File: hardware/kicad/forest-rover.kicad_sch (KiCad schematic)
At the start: 0 parts

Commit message: Refine repo wording and KiCad scaffolding
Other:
- note added: "1. Power Management"
- note added: "2. MCU Core"
- note added: "3. Motor Control"
- note added: "4. Sensor Interfaces"
- note added: "5. Communication"
- note added: "6. Connectors and Misc"
- note added: "Analog front-end: PIR buffer, threshold comparator, thermistor divider to ADC"
- note added: "Bring-up checklist: ERC cleanup, connector pinout review, footprint verification, power-tree annotation"
- note added: "Companion compute link: CM4 UART, shared I2C, GPIO interrupt, USB-C for power/data"
- note added: "DRV8871 x2 for two DC gear motors, PWM from STM32 timers, current-sense resistors, Schottky clamps"
- note added: "Encoder path: differential receiver front-end for two quadrature channels"
- note added: "I2C bus devices: BME280 and BNO055 with 4.7k pull-ups to 3.3V"
- note added: "Interfaces: UART1->CM4, UART2->LoRa, SPI1->W25Q128, I2C1->sensor bus, ADC->battery/current/temp"
- note added: "Key notes: input reverse-polarity MOSFET, 2A charge-current limit, LC output filter, soft-start"
- note added: "Layout intent: keep high di/dt loops local to the battery-side motor zone"
- note added: "Off-board headers: LIDAR UART JST-4 and thermal camera JST-6"
- note added: "Power integrity: 100nF per VDD pin plus 4.7uF bulk near MCU core rails"
- note added: "Primary rails: VBAT, +5V, +3V3, MOTOR_VBAT"
- note added: "RF placement intent: module and SMA at board edge with controlled return path"
- note added: "RFM95W LoRa module on SPI, edge-mount SMA, PI matching network, interrupt/DIO routing to MCU"
- note added: "STM32F407VGT6, 8MHz HSE, 32.768kHz LSE, SWD 2x5 1.27mm, BOOT0 jumper, GPIO expansion header"
- note added: "Status LEDs: power, charging, fault, comms; latching pushbutton; four M3 mounting holes"
- note added: "This schematic remains a structured concept. Replace each block with captured circuitry before fabrication."
- note added: "XT60 battery input, solar terminal, LT3652-style charger, TPS54331 5V buck, AMS1117-3.3, TPS2596 motor eFuse"
- note removed: "1. Power Management: solar input, LT3652-style MPPT, TPS54331 buck, AMS1117 LDO, TPS2596 motor eFuse"
- note removed: "2. MCU Core: STM32F407VGT6, crystals, SWD, BOOT0, UART/SPI/I2C/ADC breakouts"
- note removed: "3. Motor Control: DRV8871 x2, current sense, encoder receiver inputs"
- note removed: "4. Sensor Interfaces: BME280, BNO055, PIR analog front-end, thermistor divider, JST sensor headers"
- note removed: "5. Communication: RFM95W + SMA + PI match placeholder, CM4 UART/I2C/INT/USB-C"
- note removed: "6. Connectors and Misc: XT60, solar terminal, LEDs, switch, mounting holes"
- note removed: "Hierarchical block plan:"
- note removed: "This file is a hand-authored KiCad scaffold and should be replaced with a full schematic during capture."
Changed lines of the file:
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@@
   (version 20230121)
   (generator "codex")
-  (uuid "5c8ae4a4-f6bb-4f43-a6ef-forest-rover-sch")
   (paper "A3")
   (title_block
@@
     (company "Team Onyx India")
     (rev "A")
-    (comment 1 "Simplified portfolio schematic scaffold")
-    (comment 2 "Blocks: power, MCU, motors, sensors, comms"))
-  (sheet_instances
-    (path "/" (page "1")))
-  (text "Hierarchical block plan:" (at 40 30 0))
-  (text "1. Power Management: solar input, LT3652-style MPPT, TPS54331 buck, AMS1117 LDO, TPS2596 motor eFuse" (at 40 40 0))
-  (text "2. MCU Core: STM32F407VGT6, crystals, SWD, BOOT0, UART/SPI/I2C/ADC breakouts" (at 40 50 0))
-  (text "3. Motor Control: DRV8871 x2, current sense, encoder receiver inputs" (at 40 60 0))
-  (text "4. Sensor Interfaces: BME280, BNO055, PIR analog front-end, thermistor divider, JST sensor headers" (at 40 70 0))
-  (text "5. Communication: RFM95W + SMA + PI match placeholder, CM4 UART/I2C/INT/USB-C" (at 40 80 0))
-  (text "6. Connectors and Misc: XT60, solar terminal, LEDs, switch, mounting holes" (at 40 90 0))
-  (text "This file is a hand-authored KiCad scaffold and should be replaced with a full schematic during capture." (at 40 110 0))
+    (comment 1 "Top-level schematic with floorplanned functional blocks")
+    (comment 2 "Capture target: KiCad 6/7 compatible hierarchy"))
+  (polyline
+    (pts
+      (xy 20 25)
+      (xy 95 25)
+      (xy 95 85)
+      (xy 20 85)
+      (xy 20 25))
+    (stroke (width 0.2) (type solid))
+    (fill (type none))
 )
+  (polyline
+    (pts
+      (xy 105 25)
+      (xy 180 25)
+      (xy 180 85)
+      (xy 105 85)
+      (xy 105 25))
+    (stroke (width 0.2) (type solid))
+    (fill (type none))
+)
+  (polyline
+    (pts
+      (xy 190 25)
+      (xy 265 25)
+      (xy 265 85)
+      (xy 190 85)
+      (xy 190 25))
+    (stroke (width 0.2) (type solid))
+    (fill (type none))
+)
+  (polyline
+    (pts
+      (xy 20 95)
+      (xy 95 95)
+      (xy 95 155)
+      (xy 20 155)
+      (xy 20 95))
+    (stroke (width 0.2) (type solid))
+    (fill (type none))
+)
+  (polyline
+    (pts
+      (xy 105 95)
+      (xy 180 95)
+      (xy 180 155)
+      (xy 105 155)
+      (xy 105 95))
+    (stroke (width 0.2) (type solid))
+    (fill (type none))
+)
+  (polyline
+    (pts
+      (xy 190 95)
+      (xy 265 95)
+      (xy 265 155)
+      (xy 190 155)
+      (xy 190 95))
+    (stroke (width 0.2) (type solid))
+    (fill (type none))
+)
+  (text "1. Power Management" (at 24 31 0)
+    (effects (font (size 2 2) (thickness 0.3)))
+)
+  (text "XT60 battery input, solar terminal, LT3652-style charger, TPS54331 5V buck, AMS1117-3.3, TPS2596 motor eFuse" (at 24 40 0)
+    (effects (font (size 1.27 1.27)))
+)
+  (text "Primary rails: VBAT, +5V, +3V3, MOTOR_VBAT" (at 24 49 0)
+    (effects (font (size 1.27 1.27)))
+)
+  (text "Key notes: input reverse-polarity MOSFET, 2A charge-current limit, LC output filter, soft-start" (at 24 58 0)
+    (effects (font (size 1.27 1.27)))
+)
+  (text "2. MCU Core" (at 109 31 0)
+    (effects (font (size 2 2) (thickness 0.3)))
+)
+  (text "STM32F407VGT6, 8MHz HSE, 32.768kHz LSE, SWD 2x5 1.27mm, BOOT0 jumper, GPIO expansion header" (at 109 40 0)
+    (effects (font (size 1.27 1.27)))
+)
+  (text "Interfaces: UART1->CM4, UART2->LoRa, SPI1->W25Q128, I2C1->sensor bus, ADC->battery/current/temp" (at 109 49 0)
+    (effects (font (size 1.27 1.27)))
+)
+  (text "Power integrity: 100nF per VDD pin plus 4.7uF bulk near MCU core rails" (at 109 58 0)
+    (effects (font (size 1.27 1.27)))
+)
+  (text "3. Motor Control" (at 194 31 0)
+    (effects (font (size 2 2) (thickness 0.3)))
+)
+  (text "DRV8871 x2 for two DC gear motors, PWM from STM32 timers, current-sense resistors, Schottky clamps" (at 194 40 0)
+    (effects (font (size 1.27 1.27)))
+)
+  (text "Encoder path: differential receiver front-end for two quadrature channels" (at 194 49 0)
+    (effects (font (size 1.27 1.27)))
+)
+  (text "Layout intent: keep high di/dt loops local to the battery-side motor zone" (at 194 58 0)
+    (effects (font (size 1.27 1.27)))
+)
+  (text "4. Sensor Interfaces" (at 24 101 0)
+    (effects (font (size 2 2) (thickness 0.3)))
+)
+  (text "I2C bus devices: BME280 and BNO055 with 4.7k pull-ups to 3.3V" (at 24 110 0)
+    (effects (font (size 1.27 1.27)))
+)
+  (text "Analog front-end: PIR buffer, threshold comparator, thermistor divider to ADC" (at 24 119 0)
+    (effects (font (size 1.27 1.27)))
+)
+  (text "Off-board headers: LIDAR UART JST-4 and thermal camera JST-6" (at 24 128 0)
+    (effects (font (size 1.27 1.27)))
+)
+  (text "5. Communication" (at 109 101 0)
+    (effects (font (size 2 2) (thickness 0.3)))
+)
+  (text "RFM95W LoRa module on SPI, edge-mount SMA, PI matching network, interrupt/DIO routing to MCU" (at 109 110 0)
+    (effects (font (size 1.27 1.27)))
+)
+  (text "Companion compute link: CM4 UART, shared I2C, GPIO interrupt, USB-C for power/data" (at 109 119 0)
+    (effects (font (size 1.27 1.27)))
+)
+  (text "RF placement intent: module and SMA at board edge with controlled return path" (at 109 128 0)
+    (effects (font (size 1.27 1.27)))
+)
+  (text "6. Connectors and Misc" (at 194 101 0)
+    (effects (font (size 2 2) (thickness 0.3)))
+)
+  (text "Status LEDs: power, charging, fault, comms; latching pushbutton; four M3 mounting holes" (at 194 110 0)
+    (effects (font (size 1.27 1.27)))
+)
+  (text "Bring-up checklist: ERC cleanup, connector pinout review, footprint verification, power-tree annotation" (at 194 119 0)
+    (effects (font (size 1.27 1.27)))
+)
+  (text "This schematic remains a structured concept. Replace each block with captured circuitry before fabrication." (at 20 171 0)
+    (effects (font (size 1.5 1.5) (thickness 0.2)))
+)
+  (path "/" (page "1"))
+)

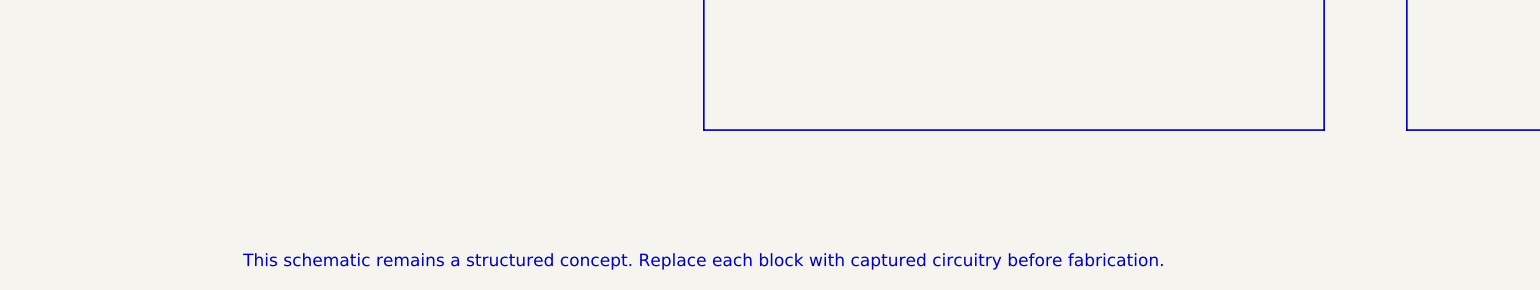
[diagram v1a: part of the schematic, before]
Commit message: Polish README and project presentation
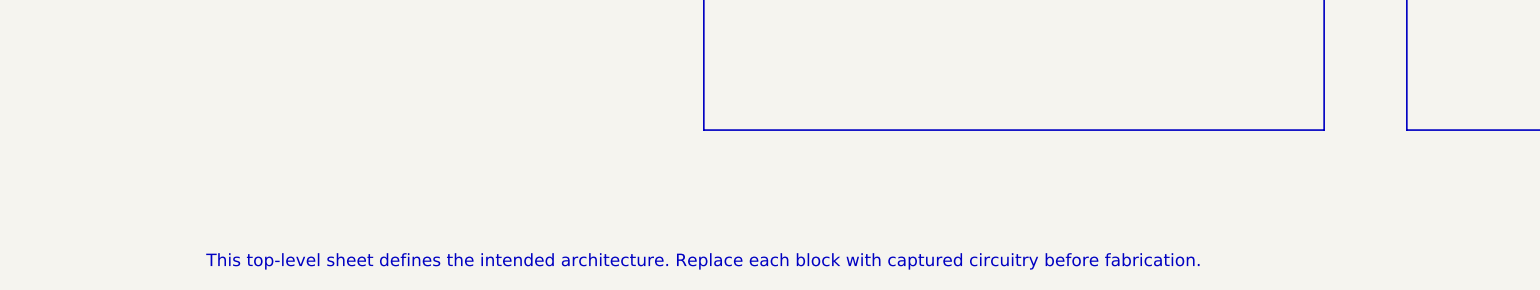
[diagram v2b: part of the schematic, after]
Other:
- note added: "This top-level sheet defines the intended architecture. Replace each block with captured circuitry before fabrication."
- note removed: "This schematic remains a structured concept. Replace each block with captured circuitry before fabrication."
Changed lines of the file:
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@@
     (effects (font (size 1.27 1.27)))
 )
-  (text "This schematic remains a structured concept. Replace each block with captured circuitry before fabrication." (at 20 171 0)
+  (text "This top-level sheet defines the intended architecture. Replace each block with captured circuitry before fabrication." (at 20 171 0)
     (effects (font (size 1.5 1.5) (thickness 0.2)))
 )
